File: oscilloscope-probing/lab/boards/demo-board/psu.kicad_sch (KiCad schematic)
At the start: 59 parts, among them J1 CONN_01X03, J2 CORTEX_DEBUG_ETM, SW1 SWITCH, SW2 SWITCH, U2 STM32L431-QFN48, U3 LTC3374A

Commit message: Finished initial demo board schematic
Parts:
- renumbered C4 to C116, C5 to C117, C6 to C118, R3 to R58
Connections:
- net 2V5 is gone; now on net 1V2: U2.13 (PA3)
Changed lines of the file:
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@@
 		)
 	)
-	(label "2V5"
+	(label "1V2"
 		(at 120.65 238.76 180)
 		(effects
@@
 		(dnp no)
 		(fields_autoplaced yes)
-		(property "Reference" "C5"
-			(at 239.141 243.0053 0)
+		(property "Reference" "C117"
+			(at 239.141 242.6278 0)
 			(effects
 				(font
@@
 		)
 		(property "Value" "0.47 uF"
-			(at 239.141 245.5422 0)
+			(at 239.141 245.0521 0)
 			(effects
 				(font
@@
 			(project "demo-board"
 				(path "/aa2d82c6-7ba7-4266-9b47-ed3339e6c556/7f5e8da7-d7e2-46c6-9076-78cb27b9675a"
-					(reference "C5")
+					(reference "C117")
 					(unit 1)
 				)
@@
 		(on_board yes)
 		(dnp no)
-		(property "Reference" "R3"
+		(property "Reference" "R58"
 			(at 41.91 252.984 90)
 			(effects
@@
 			(project "demo-board"
 				(path "/aa2d82c6-7ba7-4266-9b47-ed3339e6c556/7f5e8da7-d7e2-46c6-9076-78cb27b9675a"
-					(reference "R3")
+					(reference "R58")
 					(unit 1)
 				)
@@
 		(dnp no)
 		(fields_autoplaced yes)
-		(property "Reference" "C4"
-			(at 211.201 243.0053 0)
+		(property "Reference" "C116"
+			(at 211.201 242.6278 0)
 			(effects
 				(font
@@
 		)
 		(property "Value" "0.47 uF"
-			(at 211.201 245.5422 0)
+			(at 211.201 245.0521 0)
 			(effects
 				(font
@@
 			(project "demo-board"
 				(path "/aa2d82c6-7ba7-4266-9b47-ed3339e6c556/7f5e8da7-d7e2-46c6-9076-78cb27b9675a"
-					(reference "C4")
+					(reference "C116")
 					(unit 1)
 				)
@@
 		(dnp no)
 		(fields_autoplaced yes)
-		(property "Reference" "C6"
-			(at 212.09 262.1112 90)
+		(property "Reference" "C118"
+			(at 212.09 261.6665 90)
 			(effects
 				(font
@@
 		)
 		(property "Value" "0.1 uF"
-			(at 212.09 264.6481 90)
+			(at 212.09 264.0908 90)
 			(effects
 				(font
@@
 			(project "demo-board"
 				(path "/aa2d82c6-7ba7-4266-9b47-ed3339e6c556/7f5e8da7-d7e2-46c6-9076-78cb27b9675a"
-					(reference "C6")
+					(reference "C118")
 					(unit 1)
 				)

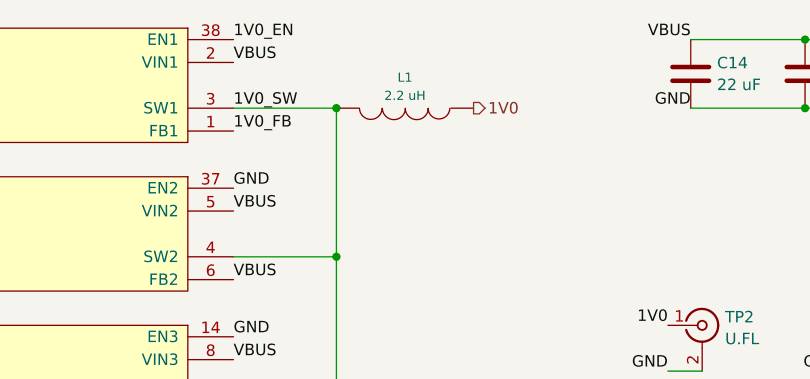
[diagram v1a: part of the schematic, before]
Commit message: Continued initial schematic, assigned footprints
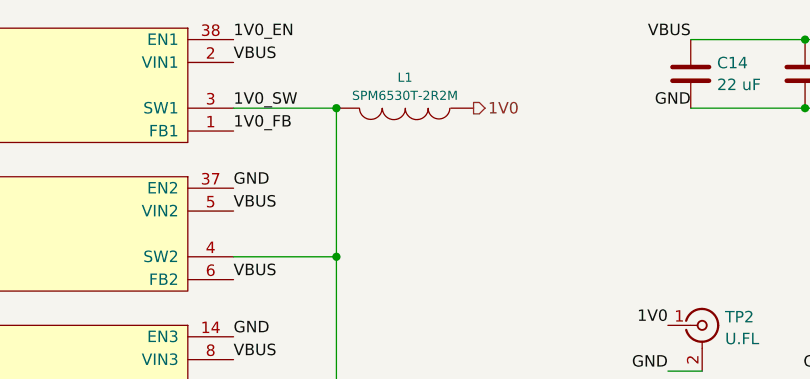
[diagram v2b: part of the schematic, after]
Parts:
- L1: value 2.2 uH -> SPM6530T-2R2M; footprint (none) -> azonenberg_pcb:INDUCTOR_TDK_SPM6530
- L2, L3, L4: footprint (none) -> azonenberg_pcb:EIA_1210_CAP_NOSILK
- R10, R11, R12, R13, R14, R15, R16, R17, R7, R8, R9: footprint (none) -> azonenberg_pcb:EIA_0402_RES_NOSILK
- TP1: footprint (none) -> azonenberg_pcb:CONN_HEADER_2.54MM_1x4
- TP2, TP3, TP4, TP5, TP6, TP7: footprint (none) -> azonenberg_pcb:CONN_U.FL_TE_1909763-1
- U2: footprint (none) -> azonenberg_pcb:QFN_48_0.5MM_7x7MM
- U3: footprint (none) -> azonenberg_pcb:QFN_38_0.5MM_5x7MM
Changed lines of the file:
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@@
 			)
 		)
-		(property "Footprint" ""
+		(property "Footprint" "azonenberg_pcb:EIA_0402_RES_NOSILK"
 			(at 216.662 162.56 90)
 			(effects
@@
 			)
 		)
-		(property "Footprint" ""
+		(property "Footprint" "azonenberg_pcb:QFN_38_0.5MM_5x7MM"
 			(at 38.1 162.56 0)
 			(effects
@@
 					(size 1.524 1.524)
 				)
+				(hide yes)
 			)
 		)
@@
 			)
 		)
-		(property "Footprint" ""
+		(property "Footprint" "azonenberg_pcb:QFN_38_0.5MM_5x7MM"
 			(at 60.96 143.51 0)
 			(effects
@@
 					(size 1.524 1.524)
 				)
+				(hide yes)
 			)
 		)
@@
 			)
 		)
-		(property "Value" "2.2 uH"
+		(property "Value" "SPM6530T-2R2M"
 			(at 85.09 22.7412 90)
 			(effects
@@
 			)
 		)
-		(property "Footprint" ""
+		(property "Footprint" "azonenberg_pcb:INDUCTOR_TDK_SPM6530"
 			(at 85.09 24.13 0)
 			(effects
@@
 					(size 1.524 1.524)
 				)
+				(hide yes)
 			)
 		)
@@
 			)
 		)
-		(property "Footprint" ""
+		(property "Footprint" "azonenberg_pcb:CONN_U.FL_TE_1909763-1"
 			(at 191.77 48.26 0)
 			(effects
@@
 			)
 		)
-		(property "Footprint" ""
+		(property "Footprint" "azonenberg_pcb:EIA_0402_RES_NOSILK"
 			(at 196.342 152.4 90)
 			(effects
@@
 			)
 		)
-		(property "Footprint" ""
+		(property "Footprint" "azonenberg_pcb:CONN_U.FL_TE_1909763-1"
 			(at 173.99 48.26 0)
 			(effects
@@
 			)
 		)
-		(property "Footprint" ""
+		(property "Footprint" "azonenberg_pcb:QFN_38_0.5MM_5x7MM"
 			(at 60.96 44.45 0)
 			(effects
@@
 					(size 1.524 1.524)
 				)
+				(hide yes)
 			)
 		)
@@
 			)
 		)
-		(property "Footprint" ""
+		(property "Footprint" "azonenberg_pcb:EIA_0402_RES_NOSILK"
 			(at 216.662 152.4 90)
 			(effects
@@
 			)
 		)
-		(property "Footprint" ""
+		(property "Footprint" "azonenberg_pcb:EIA_0402_RES_NOSILK"
 			(at 196.342 162.56 90)
 			(effects
@@
 			)
 		)
-		(property "Footprint" ""
+		(property "Footprint" "azonenberg_pcb:EIA_0402_RES_NOSILK"
 			(at 132.842 152.4 90)
 			(effects
@@
 			)
 		)
-		(property "Footprint" ""
+		(property "Footprint" "azonenberg_pcb:QFN_38_0.5MM_5x7MM"
 			(at 60.96 77.47 0)
 			(effects
@@
 					(size 1.524 1.524)
 				)
+				(hide yes)
 			)
 		)
@@
 			)
 		)
-		(property "Footprint" ""
+		(property "Footprint" "azonenberg_pcb:QFN_48_0.5MM_7x7MM"
 			(at 124.46 196.85 0)
 			(effects
@@
 			)
 		)
-		(property "Footprint" ""
+		(property "Footprint" "azonenberg_pcb:CONN_U.FL_TE_1909763-1"
 			(at 209.55 48.26 0)
 			(effects
@@
 			)
 		)
-		(property "Footprint" ""
+		(property "Footprint" "azonenberg_pcb:EIA_0402_RES_NOSILK"
 			(at 155.702 152.4 90)
 			(effects
@@
 			)
 		)
-		(property "Footprint" ""
+		(property "Footprint" "azonenberg_pcb:QFN_38_0.5MM_5x7MM"
 			(at 60.96 110.49 0)
 			(effects
@@
 					(size 1.524 1.524)
 				)
+				(hide yes)
 			)
 		)
@@
 			)
 		)
-		(property "Footprint" ""
+		(property "Footprint" "azonenberg_pcb:QFN_38_0.5MM_5x7MM"
 			(at 60.96 93.98 0)
 			(effects
@@
 					(size 1.524 1.524)
 				)
+				(hide yes)
 			)
 		)
@@
 			)
 		)
-		(property "Footprint" ""
+		(property "Footprint" "azonenberg_pcb:EIA_0402_RES_NOSILK"
 			(at 132.842 162.56 90)
 			(effects
@@
 			)
 		)
-		(property "Footprint" ""
+		(property "Footprint" "azonenberg_pcb:EIA_0402_RES_NOSILK"
 			(at 155.702 162.56 90)
 			(effects
@@
 			)
 		)
-		(property "Footprint" ""
+		(property "Footprint" "azonenberg_pcb:CONN_U.FL_TE_1909763-1"
 			(at 118.11 48.26 0)
 			(effects
@@
 			)
 		)
-		(property "Footprint" ""
+		(property "Footprint" "azonenberg_pcb:EIA_1210_CAP_NOSILK"
 			(at 85.09 106.68 0)
 			(effects
@@
 					(size 1.524 1.524)
 				)
+				(hide yes)
 			)
 		)
@@
 			)
 		)
-		(property "Footprint" ""
+		(property "Footprint" "azonenberg_pcb:QFN_48_0.5MM_7x7MM"
 			(at 85.09 247.65 0)
 			(effects
@@
 			)
 		)
-		(property "Footprint" ""
+		(property "Footprint" "azonenberg_pcb:EIA_1210_CAP_NOSILK"
 			(at 85.09 90.17 0)
 			(effects
@@
 					(size 1.524 1.524)
 				)
+				(hide yes)
 			)
 		)
@@
 			)
 		)
-		(property "Footprint" ""
+		(property "Footprint" "azonenberg_pcb:QFN_38_0.5MM_5x7MM"
 			(at 60.96 27.94 0)
 			(effects
@@
 					(size 1.524 1.524)
 				)
+				(hide yes)
 			)
 		)
@@
 			)
 		)
-		(property "Footprint" ""
+		(property "Footprint" "azonenberg_pcb:EIA_0402_RES_NOSILK"
 			(at 176.022 162.56 90)
 			(effects
@@
 			)
 		)
-		(property "Footprint" ""
+		(property "Footprint" "azonenberg_pcb:CONN_U.FL_TE_1909763-1"
 			(at 156.21 48.26 0)
 			(effects
@@
 			)
 		)
-		(property "Footprint" ""
+		(property "Footprint" "azonenberg_pcb:EIA_0402_RES_NOSILK"
 			(at 278.13 224.028 90)
 			(effects
@@
 			)
 		)
-		(property "Footprint" ""
+		(property "Footprint" "azonenberg_pcb:EIA_0402_RES_NOSILK"
 			(at 176.022 152.4 90)
 			(effects
@@
 			)
 		)
-		(property "Footprint" ""
+		(property "Footprint" "azonenberg_pcb:CONN_U.FL_TE_1909763-1"
 			(at 137.16 48.26 0)
 			(effects
@@
 			)
 		)
-		(property "Footprint" ""
+		(property "Footprint" "azonenberg_pcb:CONN_HEADER_2.54MM_1x4"
 			(at 99.06 223.52 0)
 			(effects
@@
 			)
 		)
-		(property "Footprint" ""
+		(property "Footprint" "azonenberg_pcb:EIA_1210_CAP_NOSILK"
 			(at 85.09 123.19 0)
 			(effects
@@
 					(size 1.524 1.524)
 				)
+				(hide yes)
 			)
 		)
@@
 			)
 		)
-		(property "Footprint" ""
+		(property "Footprint" "azonenberg_pcb:QFN_48_0.5MM_7x7MM"
 			(at 124.46 247.65 0)
 			(effects
@@
 			)
 		)
-		(property "Footprint" ""
+		(property "Footprint" "azonenberg_pcb:QFN_48_0.5MM_7x7MM"
 			(at 166.37 196.85 0)
 			(effects
@@
 			)
 		)
-		(property "Footprint" ""
+		(property "Footprint" "azonenberg_pcb:QFN_38_0.5MM_5x7MM"
 			(at 60.96 127 0)
 			(effects
@@
 					(size 1.524 1.524)
 				)
+				(hide yes)
 			)
 		)
@@
 			)
 		)
-		(property "Footprint" ""
+		(property "Footprint" "azonenberg_pcb:QFN_48_0.5MM_7x7MM"
 			(at 171.45 247.65 0)
 			(effects
@@
 			)
 		)
-		(property "Footprint" ""
+		(property "Footprint" "azonenberg_pcb:QFN_38_0.5MM_5x7MM"
 			(at 60.96 60.96 0)
 			(effects
@@
 					(size 1.524 1.524)
 				)
+				(hide yes)
 			)
 		)

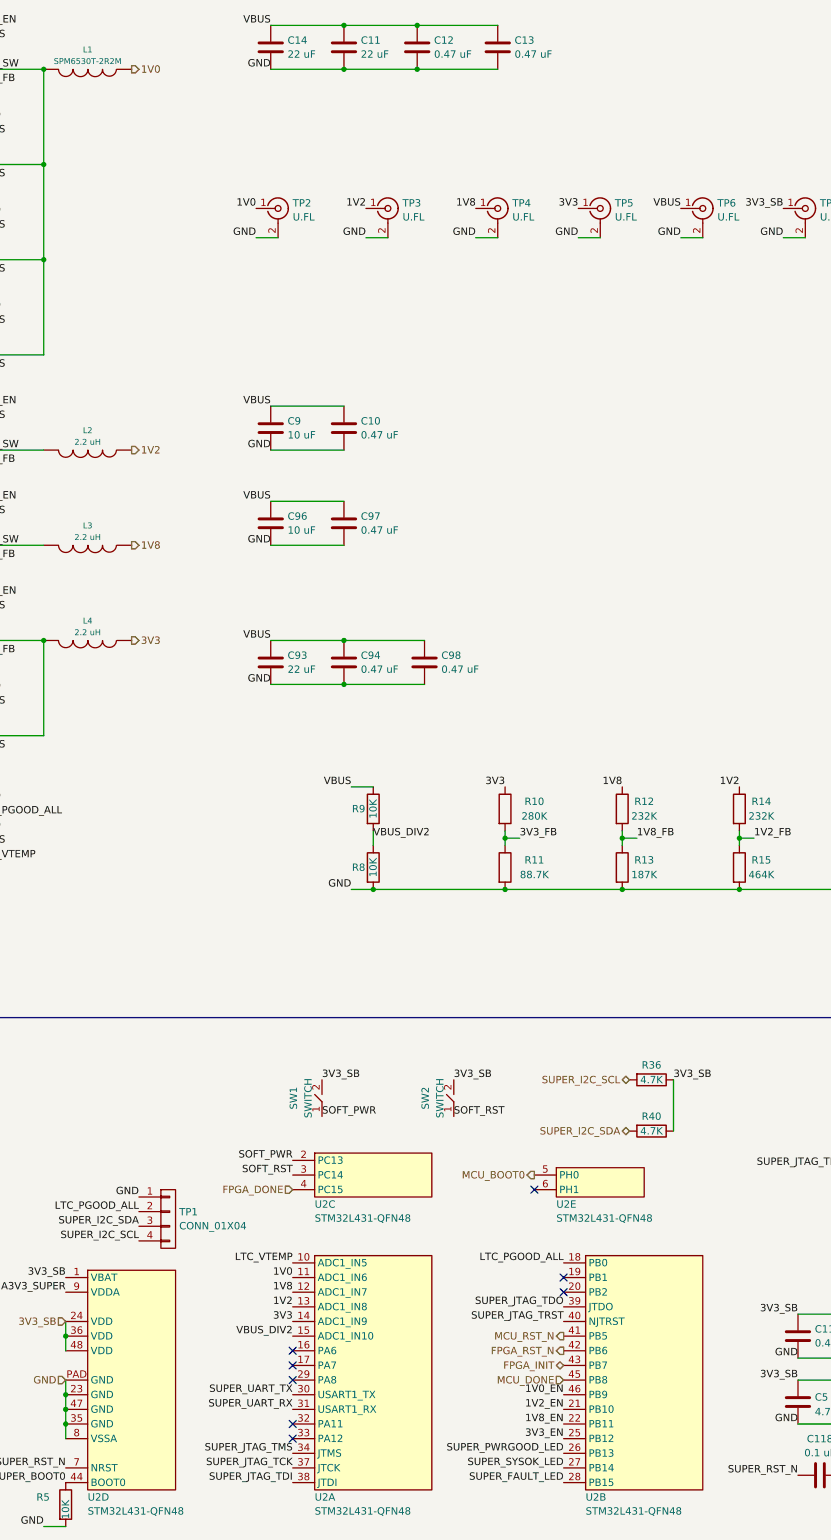
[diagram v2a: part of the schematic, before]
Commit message: Continued demo board layout
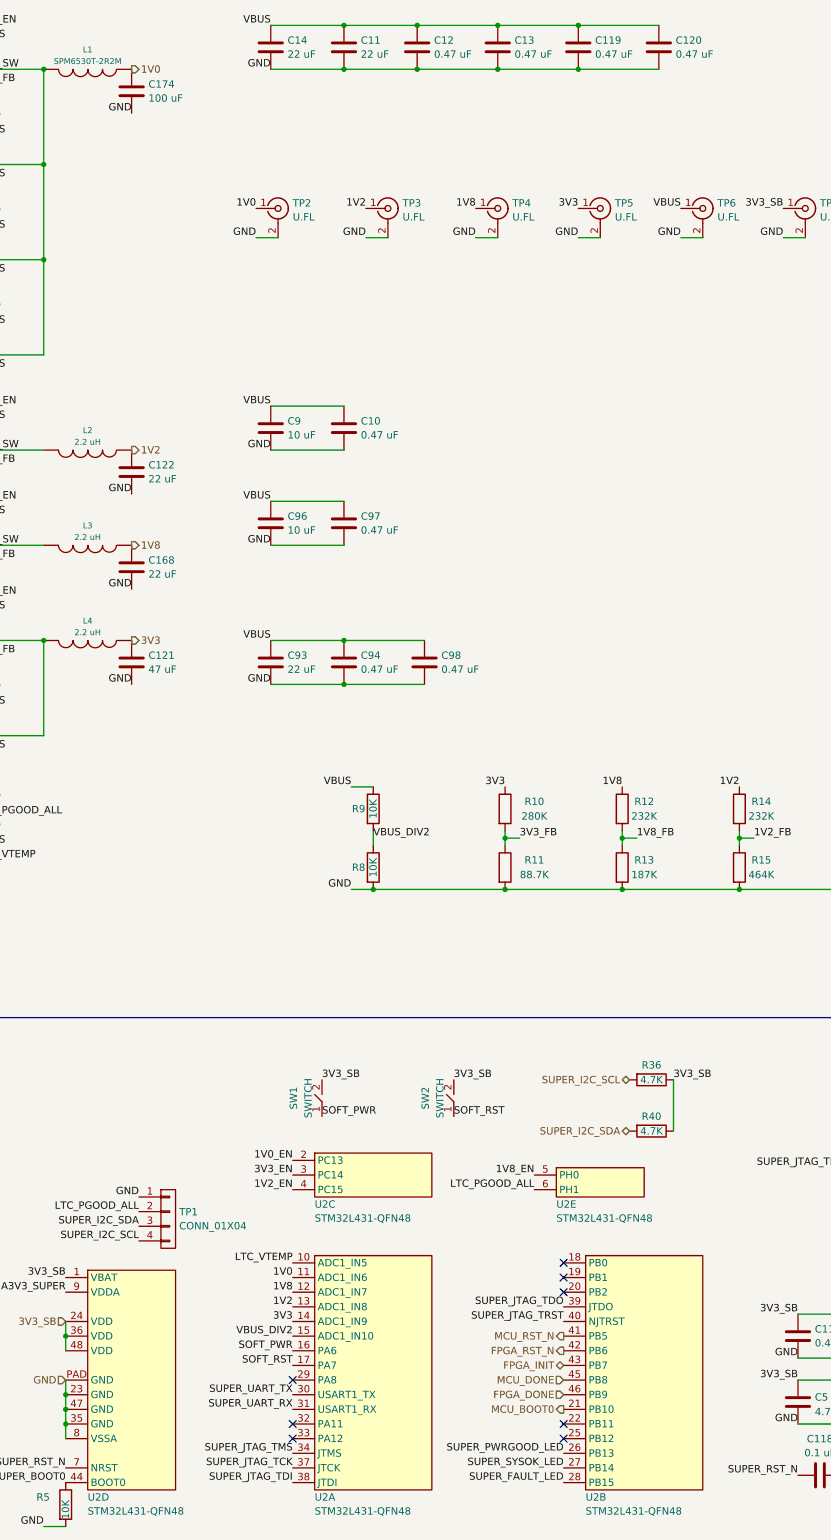
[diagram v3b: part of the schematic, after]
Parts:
- added C119, C120: 0.47 uF, azonenberg_pcb:EIA_0402_CAP_NOSILK, symbol device:C
- added C121: 47 uF, azonenberg_pcb:EIA_1210_CAP_NOSILK, symbol device:C
- added C122, C168: 22 uF, azonenberg_pcb:EIA_0805_CAP_NOSILK, symbol device:C
- added C174: 100 uF, azonenberg_pcb:EIA_1210_CAP_NOSILK, symbol device:C
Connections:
- net 1V0: now also C174.1
- net 1V0_EN: now also U2.2 (PC13); no longer U2.46 (PB9)
- net 1V2: now also C122.1
- net 1V2_EN: now also U2.4 (PC15); no longer U2.21 (PB10)
- net 1V8: now also C168.1
- net 1V8_EN: now also U2.5 (PH0); no longer U2.22 (PB11)
- net 3V3: now also C121.1
- net 3V3_EN: now also U2.3 (PC14); no longer U2.25 (PB12)
- net FPGA_DONE: now also U2.46 (PB9); no longer U2.4 (PC15)
- net GND: now also C119.2, C120.2, C121.2, C122.2, C168.2, C174.2
- net LTC_PGOOD_ALL: now also U2.6 (PH1); no longer U2.18 (PB0)
- net MCU_BOOT0: now also U2.21 (PB10); no longer U2.5 (PH0)
- net SOFT_PWR: now also U2.16 (PA6); no longer U2.2 (PC13)
- net SOFT_RST: now also U2.17 (PA7); no longer U2.3 (PC14)
- net VBUS: now also C119.1, C120.1

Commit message: Continued demo board layout
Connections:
- net MCU_BOOT0: now also U2.33 (PA12); no longer U2.21 (PB10)
- net SUPER_JTAG_TDOT: now reaches J2.6 (TDO), R7.2
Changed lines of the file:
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@@
 	)
 	(no_connect
-		(at 120.65 261.62)
+		(at 167.64 256.54)
 	)
 	(no_connect
@@
 			)
 			(justify left bottom)
+		)
+	)
+	(label "SUPER_JTAG_TDOT"
+		(at 298.45 222.25 180)
+		(effects
+			(font
+				(size 1.27 1.27)
+			)
+			(justify right bottom)
 		)
 	)
@@
 	(hierarchical_label "MCU_BOOT0"
 		(shape output)
-		(at 167.64 256.54 180)
-		(effects
-			(font
+		(at 120.65 261.62 180)
+		(effects
+			(font

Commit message: Continued demo board layout
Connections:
- net FPGA_INIT: now also U2.41 (PB5); no longer U2.43 (PB7)
- net FPGA_RST_N: now also U2.32 (PA11); no longer U2.42 (PB6)
- net MCU_RST_N: now also U2.29 (PA8); no longer U2.41 (PB5)
- net SUPER_I2C_SCL: now also U2.42 (PB6)
- net SUPER_I2C_SDA: now also U2.43 (PB7)
- no-connect marks 13 -> 11
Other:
- company: (none) -> Antikernel Labs
- title: (none) -> Oscilloscope Demo Board
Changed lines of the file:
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@@
 	(generator_version "9.0")
 	(paper "A3")
+	(title_block
+		(title "Oscilloscope Demo Board")
+		(date "2026-08-08")
+		(rev "0.1")
+		(company "Antikernel Labs")
+		(comment 1 "Andrew D. Zonenberg")
+	)
 	(text "DC-DC conversion"
 		(exclude_from_sim no)
@@
 	)
 	(no_connect
-		(at 120.65 259.08)
-	)
-	(no_connect
 		(at 298.45 245.11)
 	)
@@
 	)
 	(no_connect
-		(at 120.65 251.46)
-	)
-	(no_connect
 		(at 167.64 261.62)
 	)
@@
 		)
 	)
+	(label "SUPER_I2C_SDA"
+		(at 167.64 248.92 180)
+		(effects
+			(font
+				(size 1.27 1.27)
+			)
+			(justify right bottom)
+		)
+	)
 	(label "SUPER_PWRGOOD_LED"
 		(at 38.1 255.27 180)
@@
 		)
 	)
+	(label "SUPER_I2C_SCL"
+		(at 167.64 246.38 180)
+		(effects
+			(font
+				(size 1.27 1.27)
+			)
+			(justify right bottom)
+		)
+	)
 	(label "GND"
 		(at 58.42 255.27 0)
@@
 	(hierarchical_label "FPGA_INIT"
 		(shape bidirectional)
-		(at 167.64 248.92 180)
+		(at 167.64 243.84 180)
 		(effects
 			(font
@@
 	(hierarchical_label "MCU_RST_N"
 		(shape output)
-		(at 167.64 243.84 180)
+		(at 120.65 251.46 180)
 		(effects
 			(font
@@
 	(hierarchical_label "FPGA_RST_N"
 		(shape output)
-		(at 167.64 246.38 180)
+		(at 120.65 259.08 180)
 		(effects
 			(font
@@
 		)
 		(pin "42"
+			(alternate "I2C1_SCL")
 		)
 		(pin "19"
@@
 		)
 		(pin "43"
+			(alternate "I2C1_SDA")
 		)
 		(pin "7"
@@
 		)
 		(pin "42"
+			(alternate "I2C1_SCL")
 		)
 		(pin "19"
@@
 		)
 		(pin "43"
+			(alternate "I2C1_SDA")
 		)
 		(pin "7"
@@
 		)
 		(pin "42"
+			(alternate "I2C1_SCL")
 		)
 		(pin "19"
@@
 		)
 		(pin "43"
+			(alternate "I2C1_SDA")
 		)
 		(pin "7"
@@
 		)
 		(pin "42"
+			(alternate "I2C1_SCL")
 		)
 		(pin "19"
@@
 		)
 		(pin "43"
+			(alternate "I2C1_SDA")
 		)
 		(pin "7"
@@
 		)
 		(pin "42"
+			(alternate "I2C1_SCL")
 		)
 		(pin "19"
@@
 		)
 		(pin "43"
+			(alternate "I2C1_SDA")
 		)
 		(pin "7"

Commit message: Continued layout, 55 unrouted
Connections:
- net FPGA_INIT: now also U2.32 (PA11); no longer U2.41 (PB5)
- net FPGA_RST_N: now also U2.41 (PB5); no longer U2.32 (PA11)
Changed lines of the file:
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@@
 	(hierarchical_label "FPGA_INIT"
 		(shape bidirectional)
-		(at 167.64 243.84 180)
+		(at 120.65 259.08 180)
 		(effects
 			(font
@@
 	(hierarchical_label "FPGA_RST_N"
 		(shape output)
-		(at 120.65 259.08 180)
+		(at 167.64 243.84 180)
 		(effects
 			(font
